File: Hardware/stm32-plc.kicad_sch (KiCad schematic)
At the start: 0 parts

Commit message: schematic added
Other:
- added sheet Analog inputs (analog_inputs.kicad_sch)
- added sheet Analog outputs (analog_outputs.kicad_sch)
- added sheet CAN (can.kicad_sch)
- added sheet Control (control.kicad_sch)
- added sheet Digital outputs (digital_outputs.kicad_sch)
- added sheet Digital_Inputs (digital_inputs.kicad_sch)
- added sheet Power (power.kicad_sch)
- added sheet UART (uart.kicad_sch)
- title: (none) -> PLC ON STM

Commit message: scheme update
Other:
- sheet Control renamed Connectors
- sheet Connectors: file control.kicad_sch -> connectors.kicad_sch
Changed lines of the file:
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@@
 			(color 0 0 0 0.0000)
 		)
-		(property "Sheetname" "Control"
+		(property "Sheetname" "Connectors"
 			(at 114.3 56.4384 0)
 			(effects
@@
 			)
 		)
-		(property "Sheetfile" "control.kicad_sch"
+		(property "Sheetfile" "connectors.kicad_sch"
 			(at 114.3 95.8346 0)
 			(effects

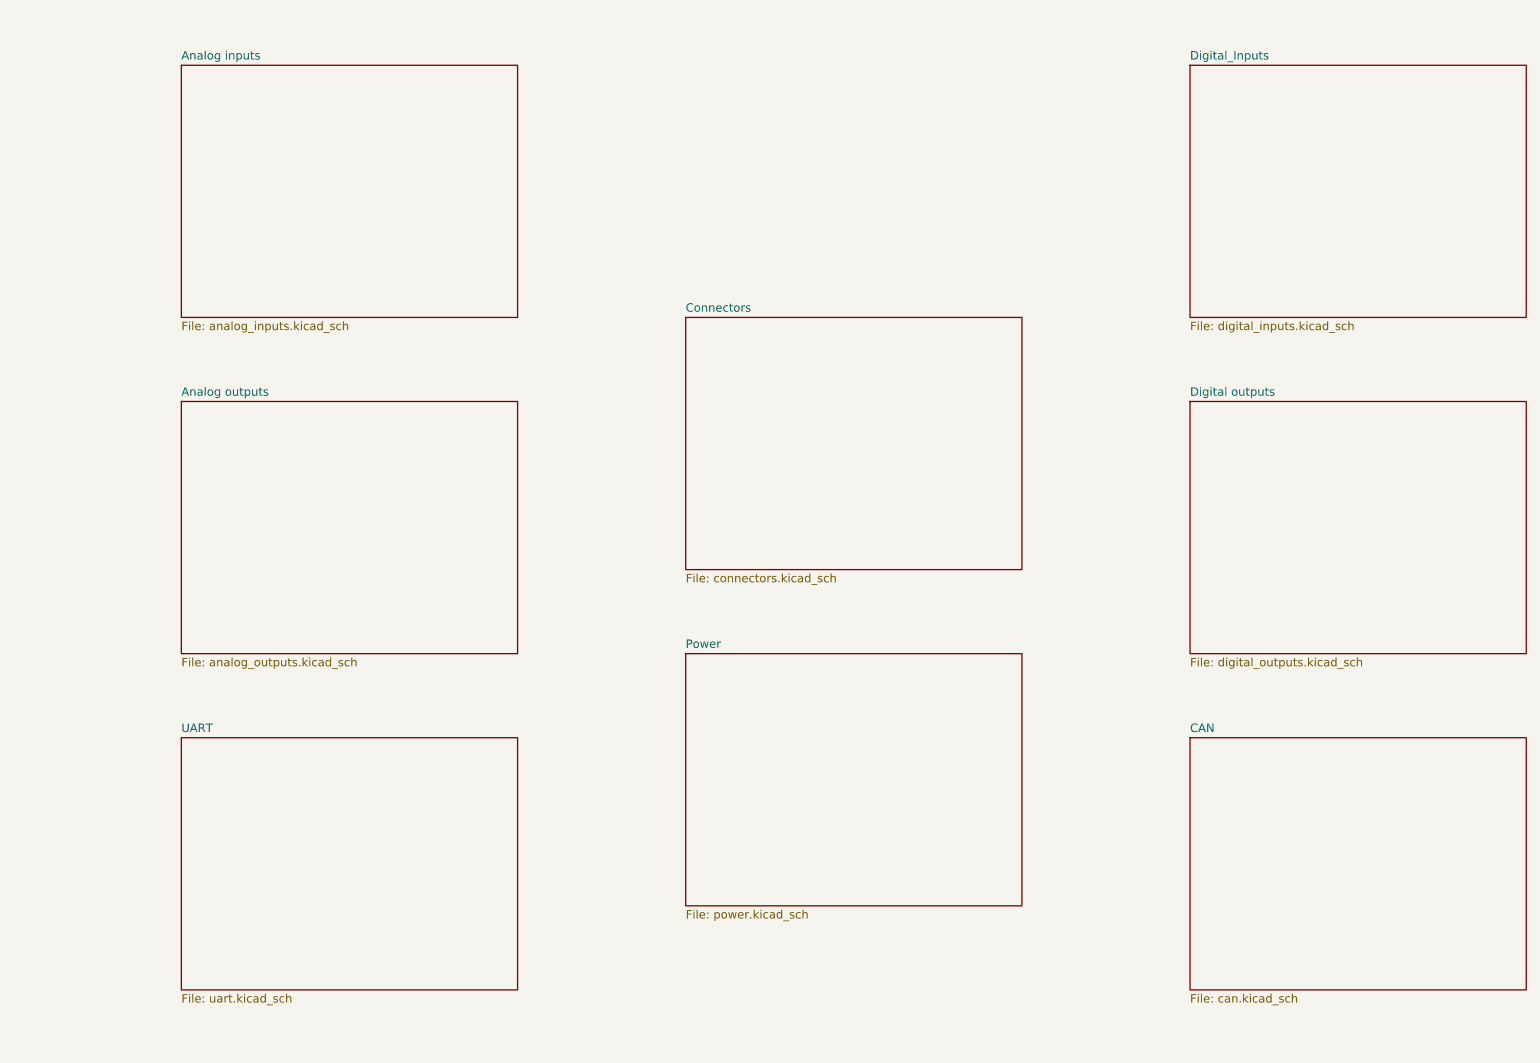
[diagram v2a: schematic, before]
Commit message: schematic update
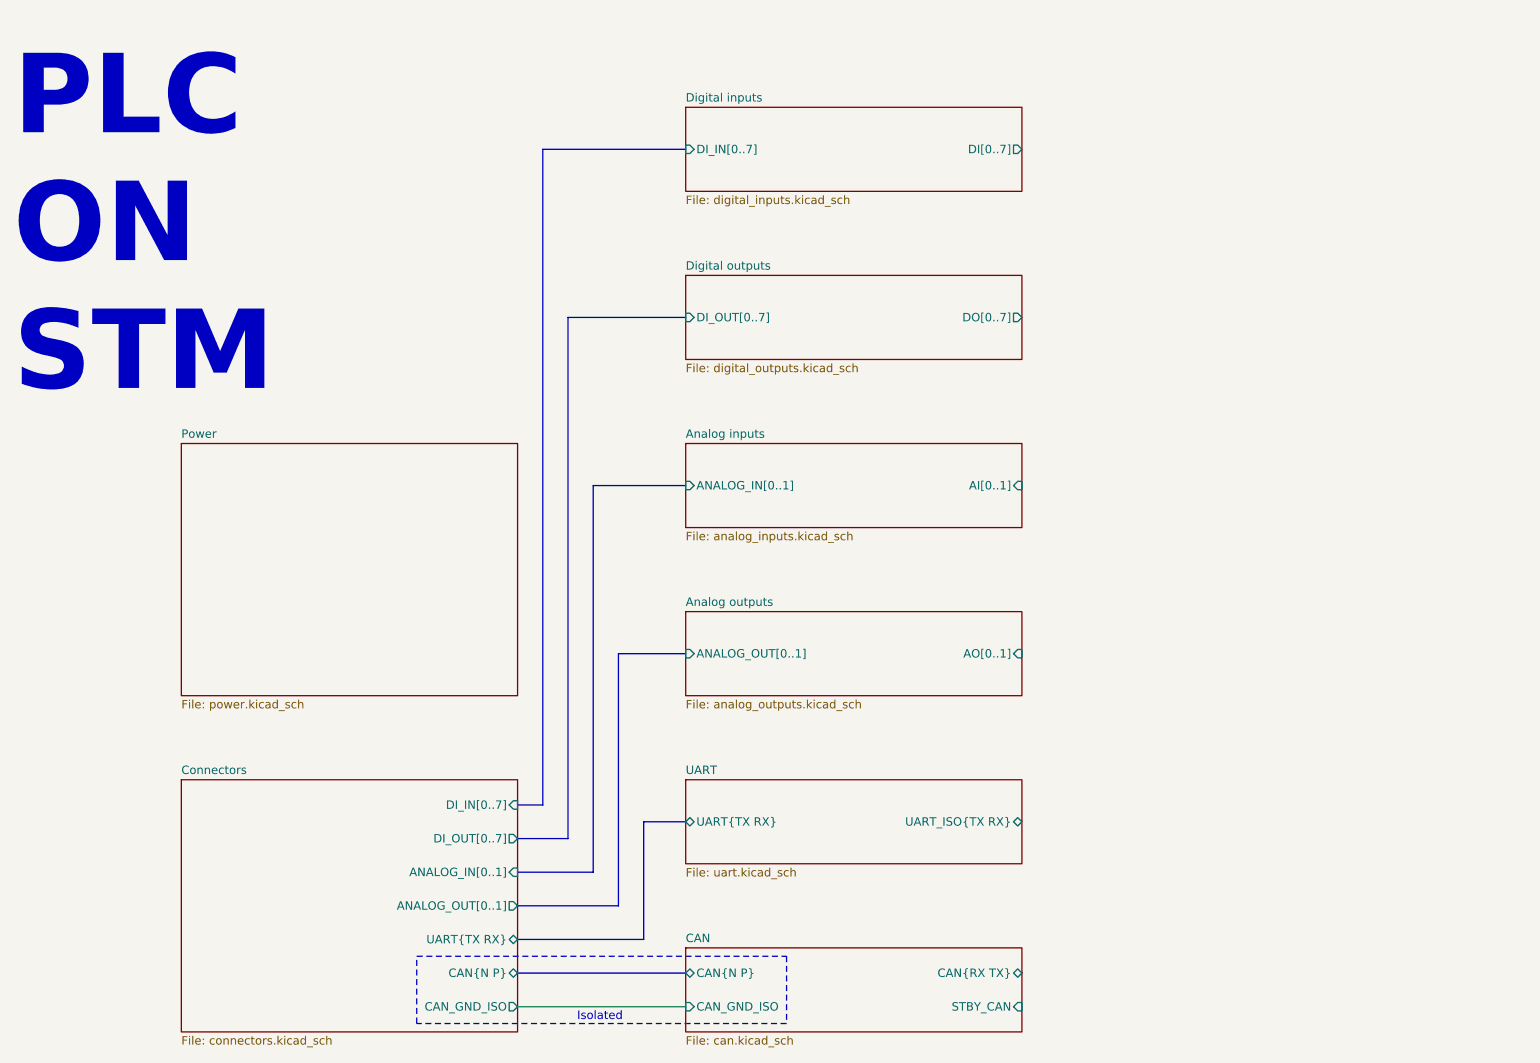
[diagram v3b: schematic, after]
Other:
- sheet Digital_Inputs renamed Digital inputs
- sheet Analog inputs ports: added AI[0..1], ANALOG_IN[0..1]; removed none
- sheet Analog outputs ports: added ANALOG_OUT[0..1], AO[0..1]; removed none
- sheet CAN ports: added CAN_GND_ISO, CAN{N P}, CAN{RX TX}, STBY_CAN; removed none
- sheet Connectors ports: added ANALOG_IN[0..1], ANALOG_OUT[0..1], CAN_GND_ISO, CAN{N P}, DI_IN[0..7], DI_OUT[0..7], UART{TX RX}; removed none
- sheet Digital inputs ports: added DI[0..7], DI_IN[0..7]; removed none
- sheet Digital outputs ports: added DI_OUT[0..7], DO[0..7]; removed none
- sheet UART ports: added UART_ISO{TX RX}, UART{TX RX}; removed none
- note added: "Isolated"
- note added: "PLC ON STM"
